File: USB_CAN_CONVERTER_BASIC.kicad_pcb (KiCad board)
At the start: 2 copper layers, 26.6 x 14.6 mm, 24 parts, among them P1 CONN_01X05, P2 CONN_01X02, P3 USB_A, P4 CONN_01X04, U1 STM32F042C6Ux, U2 PSD2CAN, U3 SN65HVD232D, U4 MCP1700T-3302E/TT, U5 USBLC6-2

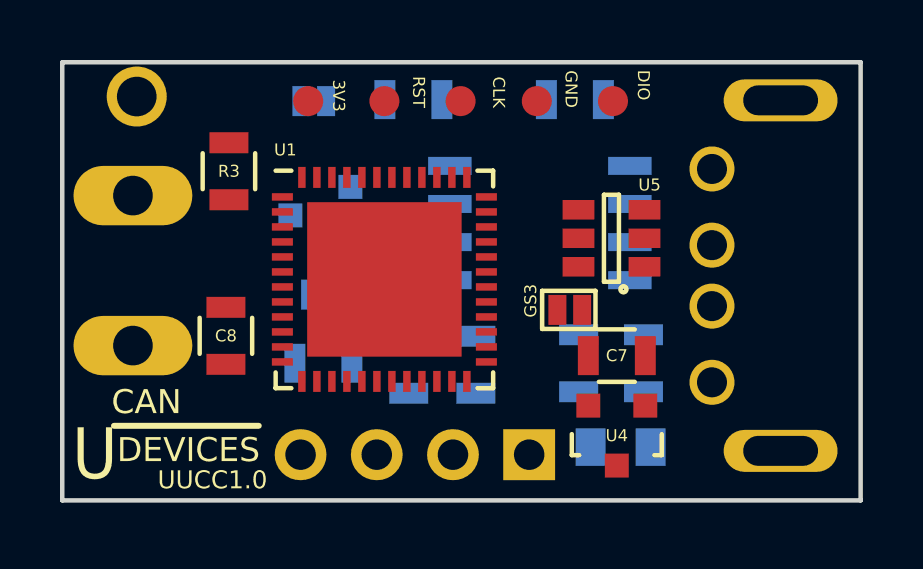
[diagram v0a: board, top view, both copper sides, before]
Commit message: Rooting and CANmod replace.
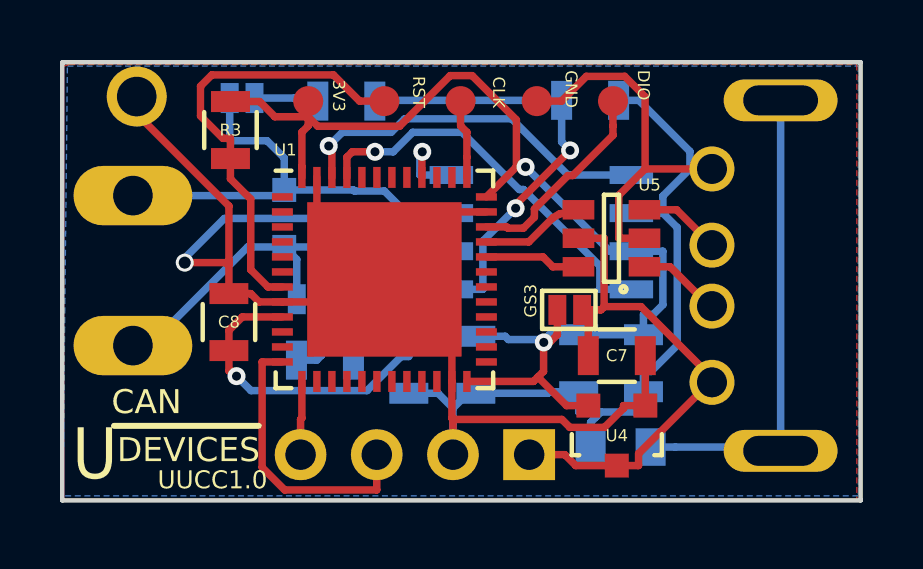
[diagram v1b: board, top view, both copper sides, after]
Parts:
- moved GS1 2.39 mm to (146.4, 93.3)
- moved R4 2.24 mm to (149.9, 93.4)
- moved R3 1.37 mm to (146.0, 94.3)
- moved GS2 0.53 mm to (148.6, 100.0), turned to 90 degrees
- moved C1 0.51 mm to (158.0, 93.3)
- moved C8 0.47 mm to (145.9, 100.7)
- moved U3 0.31 mm to (156.4, 97.7)
- moved U2 0.23 mm to (148.8, 97.3), turned to 90 degrees
- moved R5 0.11 mm to (149.1, 102.0)
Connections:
- U1 pad 40: Net-(U1-Pad40) -> CAN_MOD
- U1 pad 5: CAN_MOD -> Net-(U1-Pad5)
- U2 pad 1: Net-(GS1-Pad2) -> Net-(GS2-Pad2)
- U2 pad 2: Net-(GS2-Pad2) -> Net-(GS1-Pad2)
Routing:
- net GND: track 0.00 -> 93.7 mm, vias 0 -> 1
- net +3V3: track 0.00 -> 52.0 mm, vias 0 -> 3
- net Net-(C1-Pad2): track 0.00 -> 19.7 mm, vias 0 -> 2
- net +5V: track 0.00 -> 17.8 mm
- net Net-(L1-Pad2): track 0.00 -> 16.0 mm
- net Net-(GS2-Pad2): track 0.00 -> 15.8 mm
- net Net-(GS1-Pad2): track 0.00 -> 15.5 mm
- net Net-(P1-Pad2): track 0.00 -> 14.9 mm
- net CAN_RX: track 0.00 -> 13.1 mm, vias 0 -> 1
- net CAN_TX: track 0.00 -> 12.3 mm, vias 0 -> 1
- net /USART_TX: track 0.00 -> 9.50 mm
- net SW_DIO: track 0.00 -> 6.82 mm
- net Net-(U1-Pad33): track 0.00 -> 3.45 mm
- net Net-(U1-Pad32): track 0.00 -> 3.21 mm
- net Net-(P3-Pad2): track 0.00 -> 2.79 mm
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- added copper zone on B.Cu, net GND
- added copper zone on F.Cu, net GND

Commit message: Gerber and drill generation
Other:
- board text added: "UUCC1.1"
- board text removed: "UUCC1.0"
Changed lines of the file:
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@@
-(kicad_pcb (version 4) (host pcbnew 4.0.2-stable)
+(kicad_pcb (version 4) (host pcbnew "(2016-04-04 BZR 6663, Git 30f5a7a)-product")
   (general
     (links 79)
     (no_connects 0)
-    (area 140.316999 91.999999 167.080001 106.755001)
+    (area 139.297999 89.7205 175.477001 110.264333)
     (thickness 1.6)
     (drawings 19)
@@
     (pcbplotparams
       (layerselection 0x3ffff_ffffffff)
-      (usegerberextensions false)
+      (usegerberextensions true)
       (excludeedgelayer true)
       (linewidth 0.100000)
@@
       (hpglpenspeed 20)
       (hpglpendiameter 15)
-      (hpglpenoverlay 2)
       (psnegative false)
       (psa4output false)
@@
     (effects (font (size 0.8 0.8) (thickness 0.1)))
   )
-  (gr_text UUCC1.0 (at 145.4 106) (layer F.SilkS)
+  (gr_text UUCC1.1 (at 145.415 106.045) (layer F.SilkS)
     (effects (font (size 0.6 0.6) (thickness 0.1)))
   )
@@
   (segment (start 156.7437 98.8924) (end 156.4153 98.564) (width 0.25) (layer F.Cu) (net 14))
   (segment (start 157.599 98.8924) (end 156.7437 98.8924) (width 0.25) (layer F.Cu) (net 14))
-  (segment (start 157.599 96.9924) (end 156.972 97.1296) (width 0.25) (layer F.Cu) (net 15) (status 400000))
+  (segment (start 157.599 96.9924) (end 156.972 97.1296) (width 0.25) (layer F.Cu) (net 15))
   (segment (start 156.7437 97.263) (end 156.972 97.1296) (width 0.25) (layer F.Cu) (net 15))
   (segment (start 155.9427 98.064) (end 156.7437 97.263) (width 0.25) (layer F.Cu) (net 15))

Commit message: Fiducial Add
Fiducial Add
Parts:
- added F1: fiducial, Fiducials:Fiducial_1mm_Dia_2.54mm_Outer_CopperTop, F.Cu at (165.0, 99.2)
- added F2: fiducial, Fiducials:Fiducial_1mm_Dia_2.54mm_Outer_CopperBottom, F.Cu at (165.0, 99.2)
- U3: value SN65HVD232D -> TCAN332
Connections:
- U1 pad 30: Net-(U1-Pad30) -> CAN_MOD2
- U1 pad 49: GND -> (no net)
- U3 pad 5: Net-(C1-Pad2) -> CAN_MOD2
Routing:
- net Net-(L1-Pad2): track 16.0 -> 4.46 mm
- net CAN_MOD2: track 0.00 -> 3.82 mm, vias 0 -> 1
- net /USART_TX: track 9.50 -> 6.45 mm, vias 0 -> 1
- net Net-(C1-Pad2): track 19.7 -> 22.0 mm
- added copper zone on B.Cu, net Net-(L1-Pad2)
- added copper zone on F.Cu, net Net-(L1-Pad2)
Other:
- board text added: "UUCC1.2"
- board text removed: "UUCC1.1"

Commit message: components description update
components description update
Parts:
- removed C1: 10n, Resistors_SMD:R_0805
- removed GS2: GS2, usb_ccb_custom:GS2s
- removed R5: 60R, Resistors_SMD:R_0805
- R4: footprint Resistors_SMD:R_0805 -> Resistors_SMD:R_0402
- moved R4 6.09 mm to (148.1, 99.2), turned to 270 degrees
- moved GS1 4.16 mm to (148.1, 97.0), turned to 0 degrees
- moved U2 1.82 mm to (150.6, 97.8)
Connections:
- P2 pad 1: Net-(GS2-Pad2) -> Net-(P2-Pad1)
- R4 pad 2: Net-(C1-Pad2) -> Net-(P2-Pad1)
- U1 pad 49: (no net) -> GND
- U2 pad 1: Net-(GS2-Pad2) -> Net-(P2-Pad1)
- U3 pad 6: Net-(GS2-Pad2) -> Net-(P2-Pad1)
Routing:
- net Net-(C1-Pad2): track 22.0 -> 0.00 mm, vias 2 -> 0
- net Net-(GS2-Pad2): track 15.8 -> 0.00 mm
- net Net-(P2-Pad1): track 0.00 -> 15.0 mm
- net GND: track 93.7 -> 87.9 mm
- net Net-(GS1-Pad2): track 15.5 -> 11.0 mm
- net Net-(GS2-Pad1): track 2.77 -> 0.00 mm
- net Net-(GS1-Pad1): track 2.15 -> 1.26 mm

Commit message: Update Outputs
Update Outputs
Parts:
- U1: footprint Housings_DFN_QFN:QFN-48-1EP_7x7mm_Pitch0.5mm -> usb_ccb_custom:QFN-48-1EP_7x7mm_Pitch0.5mm
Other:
- board text added: "UCCB1.2"
- board text removed: "UUCC1.2"

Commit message: Gerber update
Gerber update
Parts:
- removed GS3: GS2, usb_ccb_custom:GS2s
- C2: footprint Resistors_SMD:R_0805 -> Capacitors_SMD:C_0805
- C3: value 10u -> 10n; footprint Resistors_SMD:R_0805 -> Capacitors_SMD:C_0805
- C4: value 10nC -> 10n; footprint Resistors_SMD:R_0805 -> Capacitors_SMD:C_0805
- C5: value 100nC -> 100n; footprint Resistors_SMD:R_0805 -> Capacitors_SMD:C_0805
- C7, C8: value 1uC -> 1u; footprint Resistors_SMD:R_0805 -> Capacitors_SMD:C_0805
- R4: value 60R -> 120R; footprint Resistors_SMD:R_0402 -> Resistors_SMD:R_0603
- U2: value PSD2CAN -> PESD2CAN
- U5: value USBLC6-2 -> USBLC6-2SC6
- moved C4 3.43 mm to (154.2, 102.2)
- moved C3 3.32 mm to (157.5, 102.2)
- moved GS1 0.42 mm to (148.4, 96.8)
- moved R4 0.36 mm to (148.4, 99.0)
- moved U2 0.35 mm to (150.9, 97.8)
- moved C8 0.34 mm to (145.9, 100.4)
- moved L1 0.30 mm to (159.0, 105.2)
- moved U3 0.14 mm to (156.5, 97.7)
- moved C2 0.09 mm to (159.8, 102.2)
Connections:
- C2 pad 1: +3V3 -> +5V
- C3 pad 1: +3V3 -> +5V
- U1 pad 1: Net-(U1-Pad1) -> (no net)
- U1 pad 10: Net-(U1-Pad10) -> (no net)
- U1 pad 11: Net-(U1-Pad11) -> (no net)
- U1 pad 14: Net-(U1-Pad14) -> (no net)
- U1 pad 15: Net-(U1-Pad15) -> (no net)
- U1 pad 16: Net-(U1-Pad16) -> (no net)
- U1 pad 17: Net-(U1-Pad17) -> (no net)
- U1 pad 18: Net-(U1-Pad18) -> (no net)
- U1 pad 19: Net-(U1-Pad19) -> (no net)
- U1 pad 2: Net-(U1-Pad2) -> (no net)
- U1 pad 20: Net-(U1-Pad20) -> (no net)
- U1 pad 21: Net-(U1-Pad21) -> (no net)
- U1 pad 22: Net-(U1-Pad22) -> (no net)
- U1 pad 25: Net-(U1-Pad25) -> (no net)
- U1 pad 26: Net-(U1-Pad26) -> (no net)
- U1 pad 27: Net-(U1-Pad27) -> (no net)
- U1 pad 28: Net-(U1-Pad28) -> (no net)
- U1 pad 29: Net-(U1-Pad29) -> (no net)
- U1 pad 3: Net-(U1-Pad3) -> (no net)
- U1 pad 31: Net-(U1-Pad31) -> (no net)
- U1 pad 38: Net-(U1-Pad38) -> (no net)
- U1 pad 39: Net-(U1-Pad39) -> (no net)
- U1 pad 4: Net-(U1-Pad4) -> (no net)
- U1 pad 41: Net-(U1-Pad41) -> (no net)
- U1 pad 42: Net-(U1-Pad42) -> (no net)
- U1 pad 43: Net-(U1-Pad43) -> (no net)
- U1 pad 44: Net-(U1-Pad44) -> (no net)
- U1 pad 5: Net-(U1-Pad5) -> (no net)
- U1 pad 6: Net-(U1-Pad6) -> (no net)
- U3 pad 3: +3V3 -> +5V
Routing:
- net +5V: track 17.8 -> 26.8 mm, vias 0 -> 1
- net GND: track 87.9 -> 96.1 mm
- net +3V3: track 52.0 -> 45.0 mm
- net Net-(GS1-Pad2): track 11.0 -> 11.8 mm
- net CAN_RX: track 13.1 -> 13.8 mm
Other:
- board text removed: "DEVICES"
